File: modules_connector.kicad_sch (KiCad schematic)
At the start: 26 parts, among them J3 Conn_01x03, J4 Conn_01x03, J5 Conn_01x03, J9 Conn_01x04, K1 HE721A0500, K2 HE721A0500, Q1 BC847, Q2 BC847

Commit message: Update
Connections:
- net Probe_L: now reaches J9.2 (Pin_2), R5.2
- net Probe_H: now reaches J9.3 (Pin_3), R25.2
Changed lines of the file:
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@@
+		)
+	)
+	(label "Probe_L"
+		(at 255.905 96.52 0)
+		(fields_autoplaced yes)
+		(effects
+			(font
+				(size 1.27 1.27)
+			)
+			(justify left bottom)
+		)
+	)
+	(label "Probe_H"
+		(at 255.905 93.98 0)
+		(fields_autoplaced yes)
+		(effects
+			(font
+				(size 1.27 1.27)
+			)
+			(justify left bottom)
 		)
 	)

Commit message: Redesign pcb
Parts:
- added C17: 100n, Capacitor_SMD:C_0603_1608Metric, symbol Koszalix_Capacitors_Ceramic_Walsin_0603:CAP_100n_X7R
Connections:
- net GND2: now also C17.2
- net Probe_H: now also J9.2 (Pin_2); no longer J9.3 (Pin_3)
- net Probe_L: now also J9.3 (Pin_3); no longer J9.2 (Pin_2)
- net VCC2: now also C17.1
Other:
- moved on the sheet: D10, D6, D7, D8, D9, J3, J4, J5, J9, K1A, K1B, K2A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

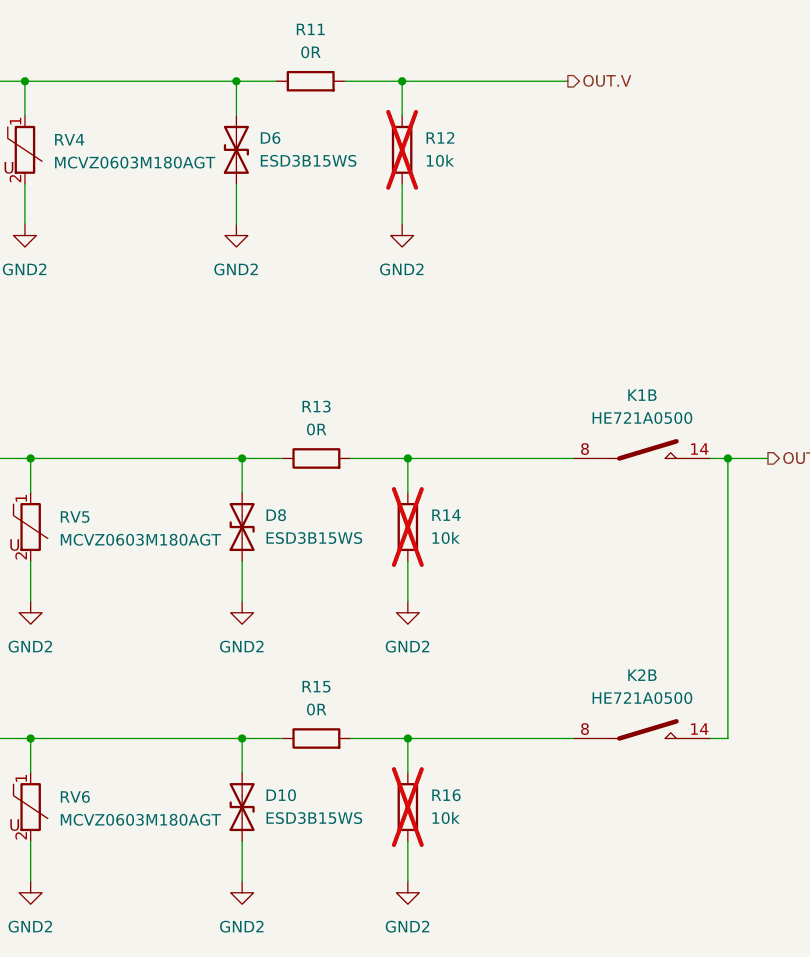
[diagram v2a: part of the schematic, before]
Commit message: Remove DNP from R12, R14, R16
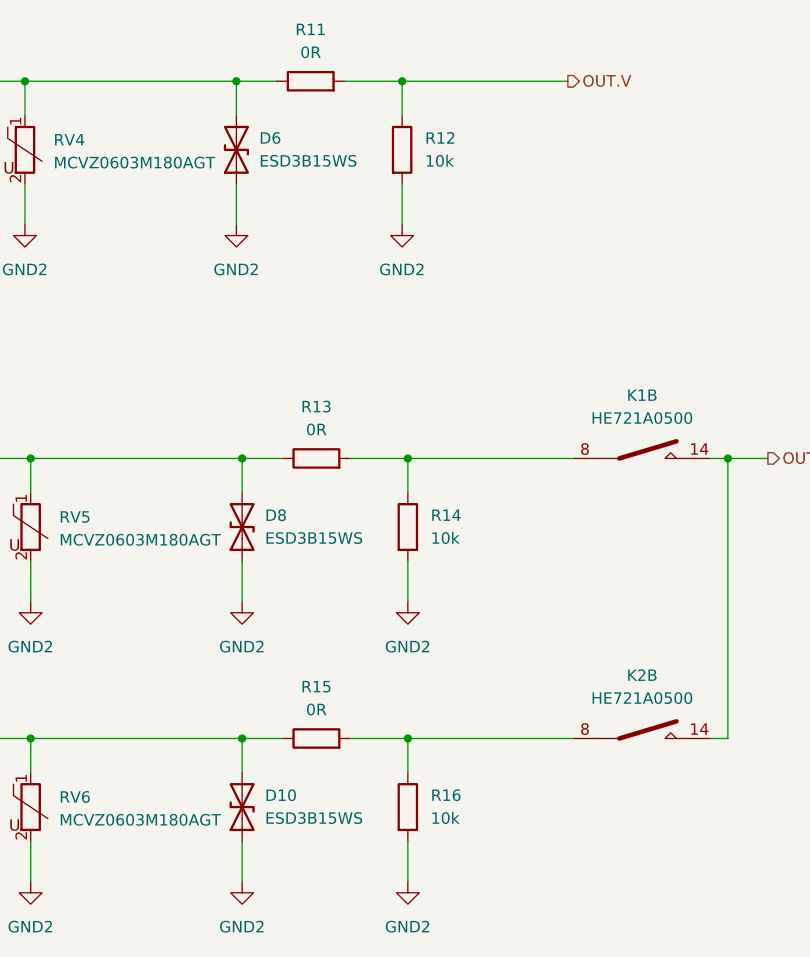
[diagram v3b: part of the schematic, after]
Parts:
- R12, R14, R16: now fitted
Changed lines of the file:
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@@
 		(in_bom yes)
 		(on_board yes)
-		(dnp yes)
+		(dnp no)
 		(fields_autoplaced yes)
 		(property "Reference" "R14"
@@
 		(in_bom yes)
 		(on_board yes)
-		(dnp yes)
+		(dnp no)
 		(fields_autoplaced yes)
 		(property "Reference" "R12"
@@
 		(in_bom yes)
 		(on_board yes)
-		(dnp yes)
+		(dnp no)
 		(fields_autoplaced yes)
 		(property "Reference" "R16"

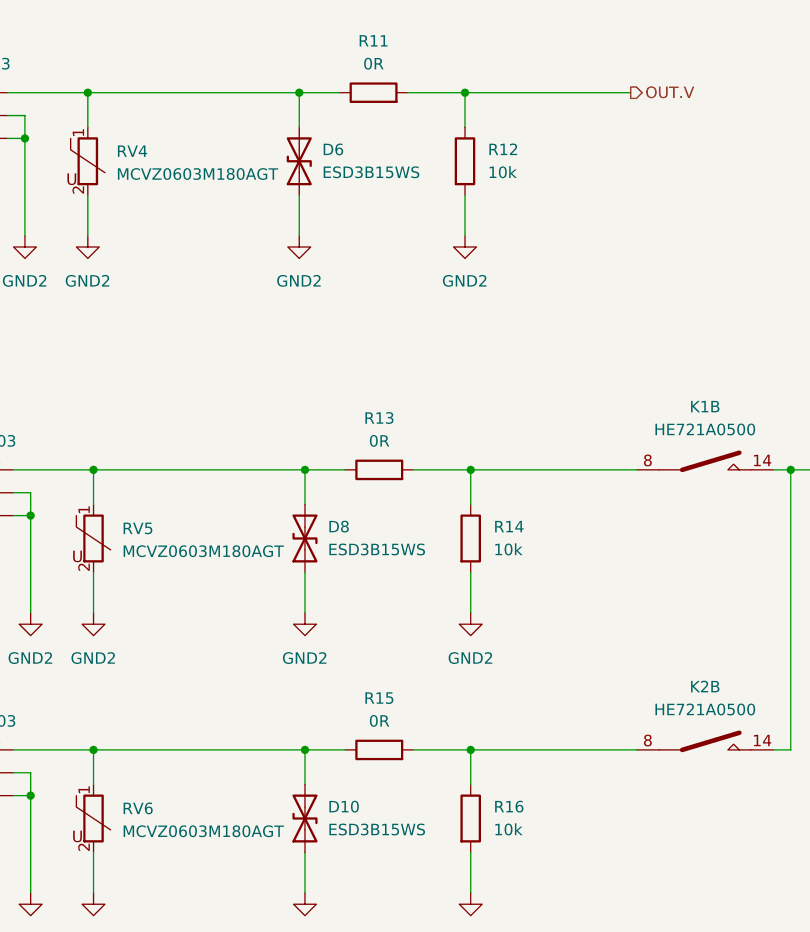
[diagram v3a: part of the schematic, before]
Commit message: Change R11, R13, R15 to 1u caps
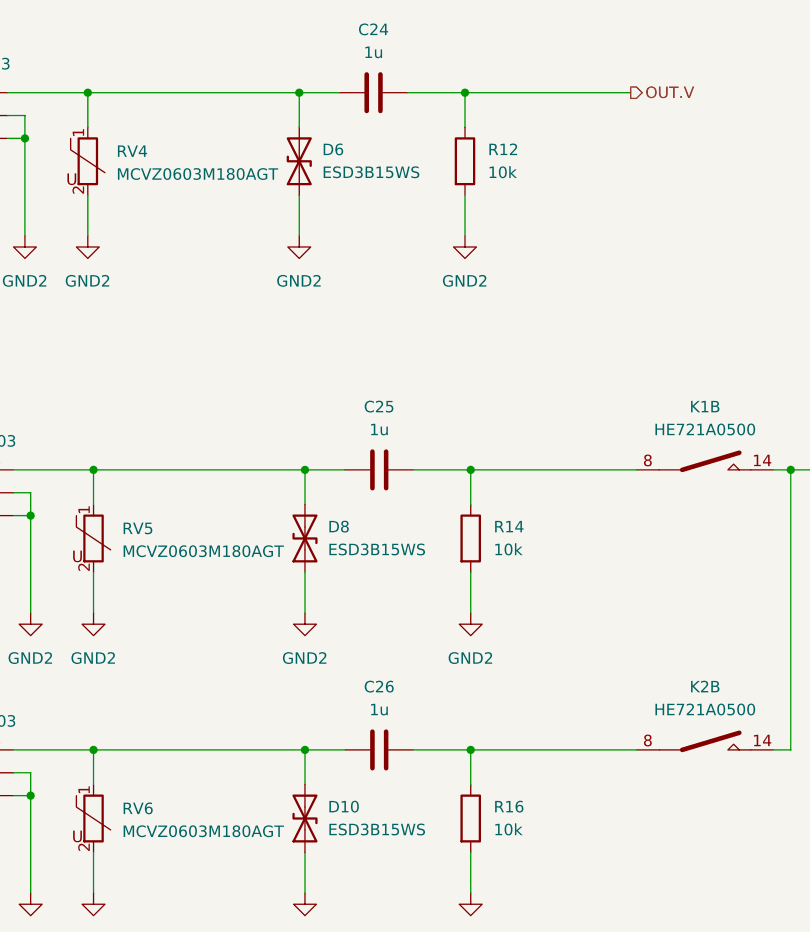
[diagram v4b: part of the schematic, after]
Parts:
- removed R11, R13, R15: 0R, Resistor_SMD:R_0603_1608Metric, symbol Koszalix_Resistors_Yageo_RC0603:RES_10k_0603
- added C24, C25, C26: 1u, Capacitor_SMD:C_0603_1608Metric, symbol Koszalix_Capacitors_Ceramic_Walsin_0603:CAP_1u_X7R
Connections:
- net OUT.V: now also C24.2
- net at D10.2 (A2), J5.3 (Pin_3), RV6.1: now also C26.1
- net at K2.7, K2.8, R16.1: now also C26.2
- net at K1.7, K1.8, R14.1: now also C25.2
- net at D8.2 (A2), J4.3 (Pin_3), RV5.1: now also C25.1
- net at D6.2 (A2), J3.3 (Pin_3), RV4.1: now also C24.1

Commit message: Bump revision to 1.1.0
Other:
- company: (none) -> koszalix
- title: (none) -> lineScope Isolators 
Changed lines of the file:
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@@
 	(generator_version "8.0")
 	(paper "A4")
+	(title_block
+		(title "lineScope Isolators ")
+		(date "2024-05-26")
+		(rev "Rev 1.1.0")
+		(company "koszalix")
+	)
 	(junction
 		(at 151.13 44.45)
